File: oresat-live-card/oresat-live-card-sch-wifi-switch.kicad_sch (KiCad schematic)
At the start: 40 parts, among them J11 2X1_TH_JUMPER, J15 2X1_TH_JUMPER, U24 LTC6994-1, U25 LTC6994-1, U26 SN74LVC1G32QDBVRQ1, U30 SN74LV1T34, U32 SN74LV1T34, U34 QPC1022, U35 SN74LVC1G32QDBVRQ1, U36 QPC1022, U6 SN74LVC1G04DCKR

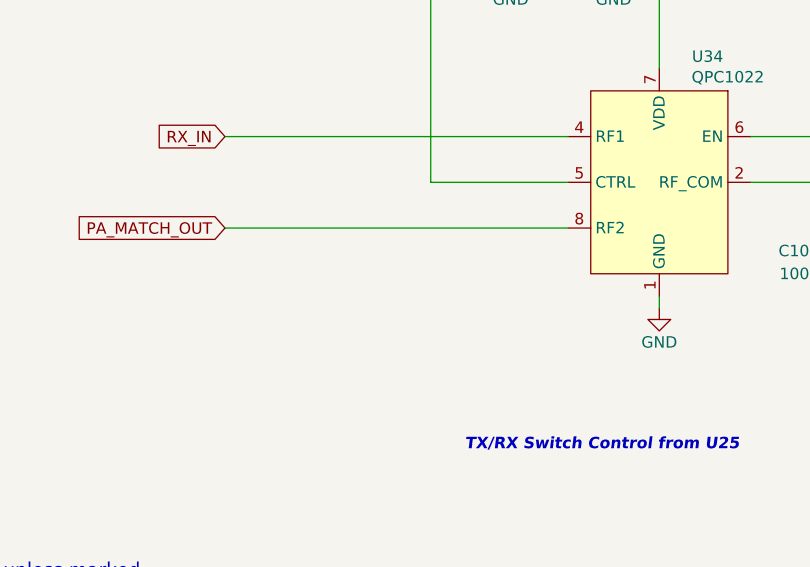
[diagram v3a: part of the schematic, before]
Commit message: added 100p cap to U34 CTRL line, some BOM changes
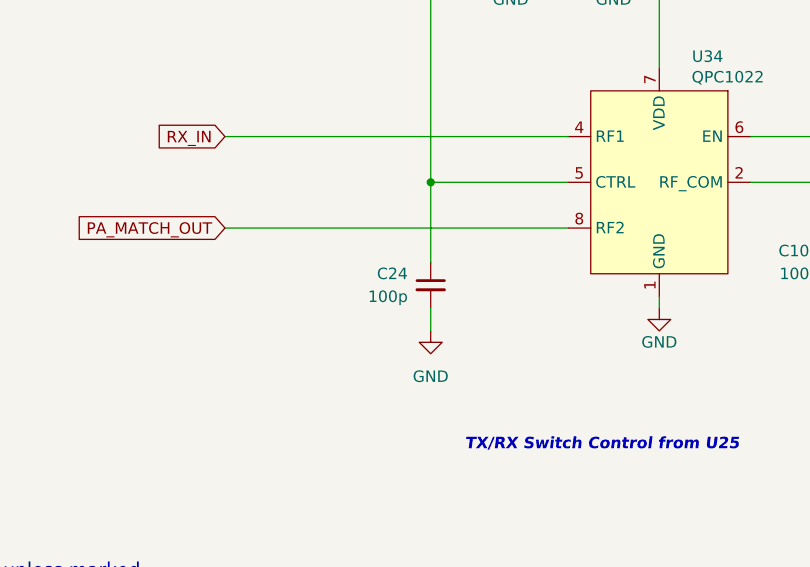
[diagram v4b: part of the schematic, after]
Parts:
- added C24: 100p, oresat-passives:0402-C, symbol Device:C_Small
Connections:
- net GND: now also C24.2
- net at R114.1, R115.1, U34.5 (CTRL): now also C24.1
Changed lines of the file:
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@@
 	)
 	(junction
+		(at 213.36 220.98)
+		(diameter 0)
+		(color 0 0 0 0)
+	)
+	(junction
 		(at 118.11 91.44)
 		(diameter 0)
@@
 	(wire
 		(pts
+			(xy 213.36 234.95) (xy 213.36 237.49)
+		)
+		(stroke
+			(width 0)
+			(type default)
+		)
+	)
+	(wire
+		(pts
 			(xy 182.88 157.48) (xy 182.88 161.29)
 		)
@@
 	(wire
 		(pts
+			(xy 213.36 220.98) (xy 213.36 229.87)
+		)
+		(stroke
+			(width 0)
+			(type default)
+		)
+	)
+	(wire
+		(pts
 			(xy 140.97 105.41) (xy 140.97 104.14)
 		)
@@
 	)
 	(symbol
+		(lib_id "power:GND")
+		(at 213.36 237.49 0)
+		(mirror y)
+		(unit 1)
+		(exclude_from_sim no)
+		(in_bom yes)
+		(on_board yes)
+		(dnp no)
+		(fields_autoplaced yes)
+		(property "Reference" "#PWR045"
+			(at 213.36 243.84 0)
+			(effects
+				(font
+					(size 1.27 1.27)
+				)
+				(hide yes)
+			)
+		)
+		(property "Value" "GND"
+			(at 213.36 242.57 0)
+			(effects
+				(font
+					(size 1.27 1.27)
+				)
+			)
+		)
+		(property "Footprint" ""
+			(at 213.36 237.49 0)
+			(effects
+				(font
+					(size 1.27 1.27)
+				)
+				(hide yes)
+			)
+		)
+		(property "Datasheet" ""
+			(at 213.36 237.49 0)
+			(effects
+				(font
+					(size 1.27 1.27)
+				)
+				(hide yes)
+			)
+		)
+		(property "Description" "Power symbol creates a global label with name \"GND\" , ground"
+			(at 213.36 237.49 0)
+			(effects
+				(font
+					(size 1.27 1.27)
+				)
+				(hide yes)
+			)
+		)
+		(pin "1"
+		)
+		(instances
+			(project "oresat-live-card"
+				(path "/748bdd2d-da0a-4240-ba60-0bf881d2ec56/7775cd78-d12a-44cc-8e12-abb8a937a463"
+					(reference "#PWR045")
+					(unit 1)
+				)
+			)
+		)
+	)
+	(symbol
 		(lib_id "Device:C_Small")
 		(at 337.82 229.87 0)
@@
 					(unit 1)
 				)
+			)
+		)
+	)
+	(symbol
+		(lib_id "Device:C_Small")
+		(at 213.36 232.41 0)
+		(mirror y)
+		(unit 1)
+		(exclude_from_sim no)
+		(in_bom yes)
+		(on_board yes)
+		(dnp no)
+		(fields_autoplaced yes)
+		(property "Reference" "C24"
+			(at 210.82 231.1462 0)
+			(effects
+				(font
+					(size 1.27 1.27)
+				)
+				(justify left)
+			)
+		)
+		(property "Value" "100p"
+			(at 210.82 233.6862 0)
+			(effects
+				(font
+					(size 1.27 1.27)
+				)
+				(justify left)
+			)
+		)
+		(property "Footprint" "oresat-passives:0402-C"
+			(at 213.36 232.41 0)
+			(effects
+				(font
+					(size 1.27 1.27)
+				)
+				(hide yes)
+			)
+		)
+		(property "Datasheet" "~"
+			(at 213.36 232.41 0)
+			(effects
+				(font
+					(size 1.27 1.27)
+				)
+				(hide yes)
+			)
+		)
+		(property "Description" "CAP CER 100PF 50V C0G/NP0 0402"
+			(at 213.36 232.41 0)
+			(effects
+				(font
+					(size 1.27 1.27)
+				)
+				(hide yes)
+			)
+		)
+		(property "DPN" "490-GCM1555C1H101GA16DCT-ND "
+			(at 213.36 232.41 0)
+			(effects
+				(font
+					(size 1.27 1.27)
+				)
+				(hide yes)
+			)
+		)
+		(property "MFR" "Murata Electronics"
+			(at 213.36 232.41 0)
+			(effects
+				(font
+					(size 1.27 1.27)
+				)
+				(hide yes)
+			)
+		)
+		(property "MPN" "GCM1555C1H101GA16D "
+			(at 213.36 232.41 0)
+			(effects
+				(font
+					(size 1.27 1.27)
+				)
+				(hide yes)
+			)
+		)
+		(property "DIS" "DigiKey"
+			(at 213.36 232.41 0)
+			(effects
+				(font
+					(size 1.27 1.27)
+				)
+				(hide yes)
+			)
+		)
+		(pin "2"
+		)
+		(pin "1"
+		)
+		(instances
+			(project "oresat-live-card"
+				(path "/748bdd2d-da0a-4240-ba60-0bf881d2ec56/7775cd78-d12a-44cc-8e12-abb8a937a463"
+					(reference "C24")
+					(unit 1)
+				)

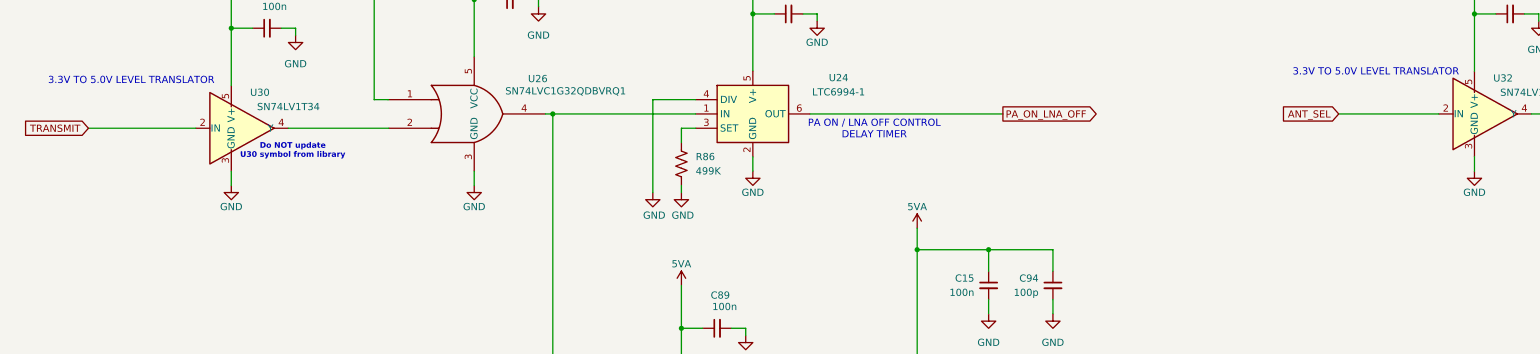
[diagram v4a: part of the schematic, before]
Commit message: added 10k pulldowns on transit and antenna switch controls pins from the octavo
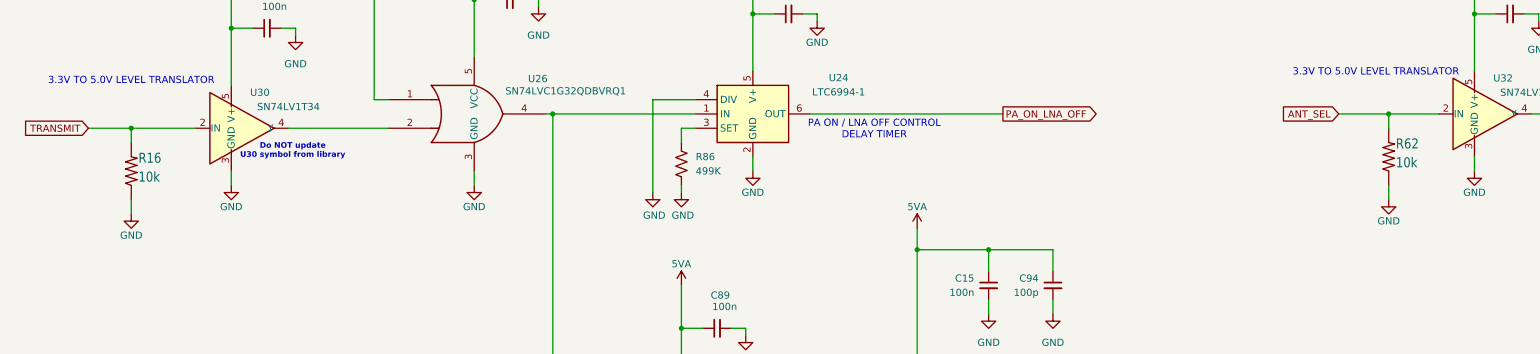
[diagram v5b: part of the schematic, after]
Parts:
- added R16, R62: 10k, oresat-passives:0603-C, symbol oresat-passives:R-US
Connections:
- net ANT_SEL: now also R62.2
- net GND: now also R16.1, R62.1
- net TRANSMIT: now also R16.2
